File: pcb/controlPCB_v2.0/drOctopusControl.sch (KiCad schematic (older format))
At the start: 74 parts, among them CON1 Servo, CON10 AVR_Prog, CON2 Servo, CON3 Heater, CON4 +12V, CON5 BEC, CON6 PIN-2x2_angled, CON7 FAN1, CON8 FAN2, CON9 UART, Q1 16MHz, SW1 RESET, T1 IRLR2905PBF, T2 IRLML6244TRPBF, T3 IRLML6244TRPBF, T4 IRLML6244TRPBF, U1 ATmega328-AU, U2 78M05CDT, U3 ESP-01, U4 AMS1117-3.3

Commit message: Working on PCBs
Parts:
- removed C11, C12: 470u/16V, Cpol_8.0_12.0_M, symbol Cpol
- removed C13, C15: 100u/25V, Cpol_6.3_11.0_N, symbol Cpol
- removed CON10: AVR_Prog, PIN-2x3_N, symbol AVR_Prog
- removed CON3: Heater, EDG-5.08mm-2_N, symbol EDG-5.08mm-2
- removed CON4: +12V, EDG-5.08mm-2_N, symbol EDG-5.08mm-2
- removed CON5: BEC, EDG-5.08mm-4_N, symbol EDG-5.08mm-4
- removed CON6: PIN-2x2_angled, PIN-2x2_angled_N, symbol PIN-2x2_angled
- removed CON7: FAN1, PIN-1x3_M, symbol PIN-1x3
- removed CON8: FAN2, PIN-1x3_M, symbol PIN-1x3
- removed CON9: UART, PIN-1x6_angled_N, symbol PIN-1x6_angled
- removed D10, D9: PESD5V2S2UT, SOT23-3_N, symbol PESD5V2S2UT
- removed D5, D6, D7, D8: SS14, SMA_N, symbol SS14
- removed Q1: 16MHz, 3.7x3.1_N, symbol Ceramic_3.7x3.1_16MHz
- removed R2: 100R, 0603_N, symbol R
- removed R5: 4k7 1%, 0603_N, symbol R
- removed R8, R9: 22R/1W, 2512_N, symbol R
- removed RN4: 1k, 4x0603_N, symbol R_Network_4
- removed RN5: 22k, 4x0603_N, symbol R_Network_4
- removed SW1: RESET, MicroswitchSmd-4.3_N, symbol MicroswitchSmt-4.3
- removed T1: IRLR2905PBF, D-PAK_N, symbol IRLR2905PBF
- removed U1: ATmega328-AU, QFP-32-0.8_M, symbol ATmega328-AU
- removed U2: 78M05CDT, D-PAK_N, symbol 78M05CDT
- removed U3: ESP-01, ESP-01_N_socket, symbol ESP-01
- added C11, C12, C13, C15, C17, C18, C19: 100n, 0603_N, symbol C
- added CON1: PIN-2x2_F, PIN-2x2_F_N, symbol PIN-2x2_F
- added CON10, CON11: Therm, PIN-2x3_N, symbol PIN-2x3
- added CON4: Outputs, PIN-2x3_N, symbol PIN-2x3
- added CON5: PIN-2x3, PIN-2x3_F_N, symbol PIN-2x3
- added CON6: PIN-2x4, PIN-2x4_F_N, symbol PIN-2x4
- added CON7: PIN-2x4, PIN-2x4_N, symbol PIN-2x4
- added D5, D6: BAS40-05(DIOTEC), SOT23-3_N, symbol BAS40-05
- added MECH9: PowerPCB, niceMechanical:dummy, symbol dummy_mech
- added Q1: Ceramic_3.7x3.1_8Mhz, 3.7x3.1_N, symbol Ceramic_3.7x3.1_8Mhz
- added R2: 10k, 0603_N, symbol R_V
- added RN5, RN6: 10k, 4x0603_N, symbol R_Network_4V
- added RN7, RN8: 10k, 4x0603_N, symbol R_Network_4
- added SW1: Button, MicroswitchSmd6x4_N, symbol MicroswitchSmt6x4_V
- added SW2: Reset, MicroswitchSmd6x4_N, symbol MicroswitchSmt6x4_V
- added U1: STM32F103RBT6, QFP-64-0.5_N, symbol STM32F103RBT6
- added U2: Oled128x64_M, niceModules:Oled128x64_M_5.08N, symbol Oled128x64_M
- CON2: footprint PIN-3x4_angled_N -> nicePinheaders:PIN-3x4_N
- CON3: renamed from CON1; footprint PIN-3x4_angled_N -> nicePinheaders:PIN-3x4_N
- R1: value 100R -> R
- R3: value 100R -> 10k
- R4: value 100R -> 1k
- RN3: value 1k -> 100R
- renumbered CON1 to CON3
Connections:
- net labels added: +3V3, BTN, DBG_RxD, DBG_TxD, ESP_RxD, ESP_TxD, HEATER, RST, SCL, SDA, SWCLK, SWDIO, SWO, Servo0, Servo0a, VDDA, cmd_heater, esp_boot, esp_en, heater_fb, therm0, therm1, therm2, therm3, therm4, therm5, therm6
- net labels removed: #DTR, #ESP, #RxD, #TxD, ESP_BOOT, ESP_EN, ESP_ENa, HEAT, Heater, MISO, MOSI, RESET, SCK, Servo8, Servo8a, Therm, uC_RxD, uC_TxD
- wire segments 220 -> 263
- no-connect marks 5 -> 4
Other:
- note added: "ADC12_IN10"
- note added: "ADC12_IN11"
- note added: "ADC12_IN12"
- note added: "ADC12_IN13"
- note added: "ADC12_IN14"
- note added: "ADC12_IN15"
- note added: "ADC12_IN4"
- note added: "ADC12_IN5"
- note added: "ADC12_IN6"
- note added: "ADC12_IN7"
- note added: "ADC12_IN8"
- note added: "ADC12_IN9"
- note added: "Buzzer\nOLED\ndebug UART\nUSB?"
- note added: "I2C2_SCL"
- note added: "I2C2_SDA"
- note added: "TIM1_CH1"
- note added: "TIM1_CH2"
- note added: "TIM1_CH3"
- note added: "TIM1_CH4"
- note added: "TIM3_CH1"
- note added: "TIM3_CH2"
- note added: "TIM3_CH3"
- note added: "TIM3_CH4"
- note added: "TIM4_CH1"
- note added: "TIM4_CH2"
- note added: "TIM4_CH3"
- note added: "TIM4_CH4"
- note added: "USART2_RX"
- note added: "USART2_TX"
- note added: "USART3_RX"
- note added: "USART3_TX"
- note added: "therm0a"
- note added: "therm1a"
- note added: "therm2a"
- note added: "therm3a"
- note added: "therm4a"
- note added: "therm5a"
- note removed: "#+5V"
- note removed: "4A max.\n0.65W max."
- note removed: "5V±5%\n300mA max.\n1.55W max."
- note removed: "8\n9\n10\n11\n12\n13\nA0\nA1\nA2\nA3\nA4\nA5\n0\n1\n2\n3\n4\n5\n6\n7"
- note removed: "A6\nA7"
- moved on the sheet: CON2A, CON2C, D11, D12, MECH1, MECH2, MECH3, MECH4, MECH5, MECH6, MECH7, MECH8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

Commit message: Schematic polishing
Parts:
- CON1: value PIN-2x2_F -> PowerPCB2
- CON5: value PIN-2x3 -> PowerPCB3
- CON6: value PIN-2x4 -> PowerPCB1
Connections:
- wire segments 263 -> 328
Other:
- note removed: "Buzzer\nOLED\ndebug UART\nUSB?"
- moved on the sheet: C1, C10, C11, C12, C13, C14, C15, C16, C17, C18, C19, C2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

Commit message: Schematic polishing
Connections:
- net LED1: now also U1.33 (PB12)
- net LED2: now also U1.34 (PB13)
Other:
- note added: "3V3 LDO regulator"
- note added: "6V power is for servos\n5V for OLED and LDO\n12V for external outputs"
- note added: "External thermistor inputs"
- note added: "For uC only"
- note added: "Mechanical parts and Power PCB"
- note added: "Medium power outputs"
- note added: "Motor and two fans"
- note added: "Power PCB connectors"
- note added: "Power PCB\nfor 3D model"
- note added: "Programming/debug connector and reset switch"
- note added: "STM32 microcontroller"
- note added: "Servo connectors"
- note added: "Servos powered from external BEC regulator"
- note added: "Thermistor 0 and 3 are for higher temperatures\nand have lower pullup resistances."
- note added: "User interaction"
- moved on the sheet: C1, C10, C11, C12, C13, C14, C15, C16, C17, C18, C19, C2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

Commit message: Schematic polishing
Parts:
- removed C4: 100n, 0603_N, symbol C
- removed R4: 1k, 0603_N, symbol R
- added R4: 1k, 0603_N, symbol R_V
- added R5: 2k2, 0603_N, symbol R
- added R6: 10k, 0603_N, symbol R
- added R7: 10k, 0603_N, symbol R_V
- added RN4: 10k, 4x0603_N, symbol R_Network_4V
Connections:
- net +3V3: no longer RN6.7 (2), RN8.4 (1)
- net BTN: no longer RN8.5 (2)
- net F1: now also D6.2 (A2); no longer D6.1 (A1)
- net F2: now also D6.1 (A1); no longer D6.2 (A2)
- net Fan1: now also RN4.5 (2)
- net Fan2: now also RN4.2 (1), RN4.6 (2), RN4.7 (2)
- net GND: now also R4.1, R7.1, RN4.1, RN4.3 (1), RN4.4 (1)
- net Motor: now also RN4.8 (2)
- net cmd_heater: now also R5.2, R7.2; no longer CON6.6
- net heater_fb: now also R4.2
- net therm0: now also RN7.8 (2); no longer RN7.1
- net therm1: now also RN7.6 (2); no longer RN7.2 (1)
- net therm2: now also RN7.5 (2); no longer RN7.3 (1)
- net therm3: now also RN8.8 (2), U1.11 (PC3); no longer RN8.1, U1.25 (PC5)
- net therm4: now also RN8.6 (2), U1.9 (PC1); no longer RN8.2 (1), U1.26 (PB0)
- net therm5: now also RN8.5 (2), U1.10 (PC2); no longer RN8.3 (1), U1.27 (PB1)
- net at C14.1, CON10.4: now also RN5.3 (1), RN7.3 (1); no longer RN5.2 (1), RN7.7 (2)
- net at C13.1, CON10.6: now also RN5.4 (1), RN7.4 (1); no longer RN5.1, RN7.6 (2)
- net at C17.1, CON11.4: now also RN6.3 (1), RN8.3 (1); no longer RN6.2 (1), RN8.7 (2)
- net at C16.1, CON11.6: now also RN6.4 (1), RN8.4 (1); no longer RN6.1, RN8.6 (2)
- new net: CON6.6, R5.1, R6.1
- new net: C15.1, CON10.2, RN5.1, RN5.2 (1), RN7.1
- new net: C18.1, CON11.2, RN6.1, RN8.1
- new net bts_fb: R6.2, U1.25 (PC5)
- no-connect marks 4 -> 8
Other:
- note added: "ADC12_IN0"
- note added: "ADC12_IN1"
- note added: "THERM0"
- note added: "Thermistor 0 is for higher temperature - for heater\nand have lower pullup resistance.\nOther are for servos and BEC"
- note removed: "Thermistor 0 and 3 are for higher temperatures\nand have lower pullup resistances."
- note removed: "therm0a"
- moved on the sheet: C19, CON4, D5, D6, RN3A, RN3B, RN3C, RN3D, RN5A, RN5B, RN5C, RN5D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

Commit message: PCB routing
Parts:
- added TP1: PA12, pnConnector:TP_1mm, symbol Testpoint
- added TP2: PB14, pnConnector:TP_1mm, symbol Testpoint
- added TP3: PB15, pnConnector:TP_1mm, symbol Testpoint
- added TP4: PA0, pnConnector:TP_1mm, symbol Testpoint
- added TP5: PA1, pnConnector:TP_1mm, symbol Testpoint
- added TP6: PB4, pnConnector:TP_1mm, symbol Testpoint
- added TP7: PB5, pnConnector:TP_1mm, symbol Testpoint
- added TP8: PC0, pnConnector:TP_1mm, symbol Testpoint
- R1, R10, R11, R2, R3, R4, R5, R6, R7: footprint 0603_N -> 0603_R_N
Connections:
- net +3V3: now also RN7.2 (1), RN7.7 (2), RN8.4 (1)
- net +5V: now also CON6.8; no longer CON6.5
- net GND: now also RN4.2 (1); no longer RN4.3 (1)
- net B2B_heater_cmd: now reaches R5.1, R6.1
- net B2B_heater_cmd: now also CON6.5; no longer CON6.6
- net at C17.1, CON11.4, RN6.3 (1): now also RN8.2 (1); no longer RN8.3 (1)
- net at C16.1, CON11.6, RN6.4 (1): now also RN8.3 (1); no longer RN8.4 (1)
- net fan2_cmd: now reaches RN3.2 (1)
- net fan2_cmd: now also RN4.7 (2), U1.39 (PC8)
- net at RN3.7 (2): now also T4.1 (G)
- net at RN3.6 (2): no longer T4.1 (G)
- net B2B_esp_boot: now reaches U1.26 (PB0)
- net B2B_esp_boot: now also CON6.3
- net B2B_esp_en: now reaches U1.27 (PB1)
- net B2B_esp_en: now also CON6.1
- net button_sig: now reaches U1.50 (PA15)
- net button_sig: now also RN8.5 (2), SW1.2
- net therm4_sig: now reaches RN8.7 (2)
- net therm4_sig: now also U1.10 (PC2)
- net BTN: no longer names the net of U1.57 (PB5)
- net BTN: no longer SW1.2
- net ESP_RxD renamed B2B_ESP_RxD
- net B2B_ESP_RxD: now also CON6.4; no longer CON6.3
- net ESP_TxD renamed B2B_ESP_TxD
- net B2B_ESP_TxD: now also CON6.2; no longer CON6.1
- net F1 renamed FAN1_OUT
- net F2 renamed FAN2_OUT
- net Fan1 renamed fan1_cmd
- net fan1_cmd: now also U1.38 (PC7); no longer U1.39 (PC8)
- removed net Fan2: RN3.3 (1), RN4.2 (1), RN4.6 (2), RN4.7 (2), U1.40 (PC9)
- net HEATER renamed B2B_heater_out
- net B2B_heater_out: now also CON6.7; no longer CON6.8
- net LED1 renamed led1_cmd
- net LED2 renamed led2_cmd
- net MOT renamed MOTOR_OUT
- net Motor renamed motor_cmd
- net motor_cmd: now also U1.40 (PC9); no longer U1.38 (PC7)
- net SCL renamed scl
- net SDA renamed sda
- net Servo0 renamed servo0_cmd
- net Servo0a renamed SERVO0_OUT
- net Servo1 renamed servo1_cmd
- net Servo1a renamed SERVO1_OUT
- net Servo2 renamed servo2_cmd
- net Servo2a renamed SERVO2_OUT
- net Servo3 renamed servo3_cmd
- net Servo3a renamed SERVO3_OUT
- net Servo4 renamed servo4_cmd
- net servo4_cmd: now also U1.61 (PB8); no longer U1.58 (PB6)
- net Servo4a renamed SERVO4_OUT
- net Servo5 renamed servo5_cmd
- net Servo5a renamed SERVO5_OUT
- net Servo6 renamed servo6_cmd
- net servo6_cmd: now also U1.58 (PB6); no longer U1.61 (PB8)
- net Servo6a renamed SERVO6_OUT
- net Servo7 renamed servo7_cmd
- net Servo7a renamed SERVO7_OUT
- net bts_fb renamed bts_fb_sig
- net cmd_heater renamed heater_cmd
- net esp_boot: no longer names the net of U1.15 (PA1)
- net esp_boot: no longer CON6.4
- net esp_en: no longer names the net of U1.14 (PA0/WKUP)
- net esp_en: no longer CON6.2
- net heater_fb renamed heater_sig
- net heater_sig: now also U1.21 (PA5); no longer U1.20 (PA4)
- net therm0 renamed therm0_sig
- net therm1 renamed therm1_sig
- net therm2 renamed therm2_sig
- net therm3 renamed therm3_sig
- net therm3_sig: now also U1.9 (PC1); no longer U1.11 (PC3)
- net therm4 renamed therm5_sig
- net therm5_sig: now also U1.11 (PC3); no longer U1.9 (PC1)
- removed net therm5: RN8.5 (2), U1.10 (PC2)
- removed net therm6: CON6.7, U1.21 (PA5)
- new net B2B_therm6_sig: CON6.6, U1.20 (PA4)
- no-connect marks 8 -> 10
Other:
- note added: "Naming convention:\n- small_letters (_cmd,_sig) - board level signals\n (out/in from uC)\n- BIG_LETTERS (_OUT,_IN) - connections to outside world\n- B2B_signals - connections to second board"
- note added: "THERM0_IN"
- note added: "THERM1_IN"
- note added: "THERM2_IN"
- note added: "THERM3_IN"
- note added: "THERM4_IN"
- note added: "THERM5_IN"
- note added: "motor_cmd and two fans"
- note removed: "Motor and two fans"
- note removed: "THERM0"
- note removed: "therm1a"
- note removed: "therm2a"
- note removed: "therm3a"
- note removed: "therm4a"
- note removed: "therm5a"
- moved on the sheet: C10, C14, C15, C17, C18, C7, C8, C9, CON10, CON11, CON2A, CON2B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

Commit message: Probably final version of PCBs
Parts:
- added CON8, CON9: GND, PIN-1x1_L, symbol PIN-1x1
- added MECH10: spacer_M3x5+6, niceMechanical:spacer_2x5_plastic, symbol spacer_M3x5+6
- added SW3: Button, MicroswitchSmd6x4_N, symbol MicroswitchSmt6x4_V
- added TP10: Fan1, pnConnector:TP_1mm, symbol Testpoint
- added TP11: Fan2, pnConnector:TP_1mm, symbol Testpoint
- added TP12: S0, pnConnector:TP_1mm, symbol Testpoint
- added TP13: S1, pnConnector:TP_1mm, symbol Testpoint
- added TP14: S2, pnConnector:TP_1mm, symbol Testpoint
- added TP15: S3, pnConnector:TP_1mm, symbol Testpoint
- added TP16: S4, pnConnector:TP_1mm, symbol Testpoint
- added TP17: S5, pnConnector:TP_1mm, symbol Testpoint
- added TP18: S6, pnConnector:TP_1mm, symbol Testpoint
- added TP19: S7, pnConnector:TP_1mm, symbol Testpoint
- added TP9: Motor, pnConnector:TP_1mm, symbol Testpoint
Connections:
- net +3V3: no longer RN8.4 (1)
- net GND: now also CON8.1, CON9.1, SW3.1
- net fan1_cmd: now also TP10.1
- net fan2_cmd: now also TP11.1
- net motor_cmd: now also TP9.1
- net servo0_cmd: now also TP12.1
- net servo1_cmd: now also TP13.1
- net servo2_cmd: now also TP14.1
- net servo3_cmd: now also TP15.1
- net servo4_cmd: now also TP16.1
- net servo5_cmd: now also TP17.1
- net servo6_cmd: now also TP18.1
- net servo7_cmd: now also TP19.1
- net at U1.14 (PA0/WKUP): now also TP4.1
- net at U1.15 (PA1): now also TP5.1
- net at U1.35 (PB14): now also TP2.1
- net at U1.36 (PB15): now also TP3.1
- net at U1.45 (PA12): now also TP1.1
- net at U1.56 (PB4): now also TP6.1
- net at U1.57 (PB5): now also TP7.1
- net button1_sig: now reaches U1.53 (PC12)
- net button1_sig: now also SW3.2
- net at U1.8 (PC0): now also TP8.1
- net button_sig renamed button0_sig
- net button0_sig: no longer RN8.5 (2)
- no-connect marks 10 -> 13
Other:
- moved on the sheet: C10, C6, C9, CON2A, CON2B, CON2C, CON3A, CON3B, CON3C, CON7, D1, D11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

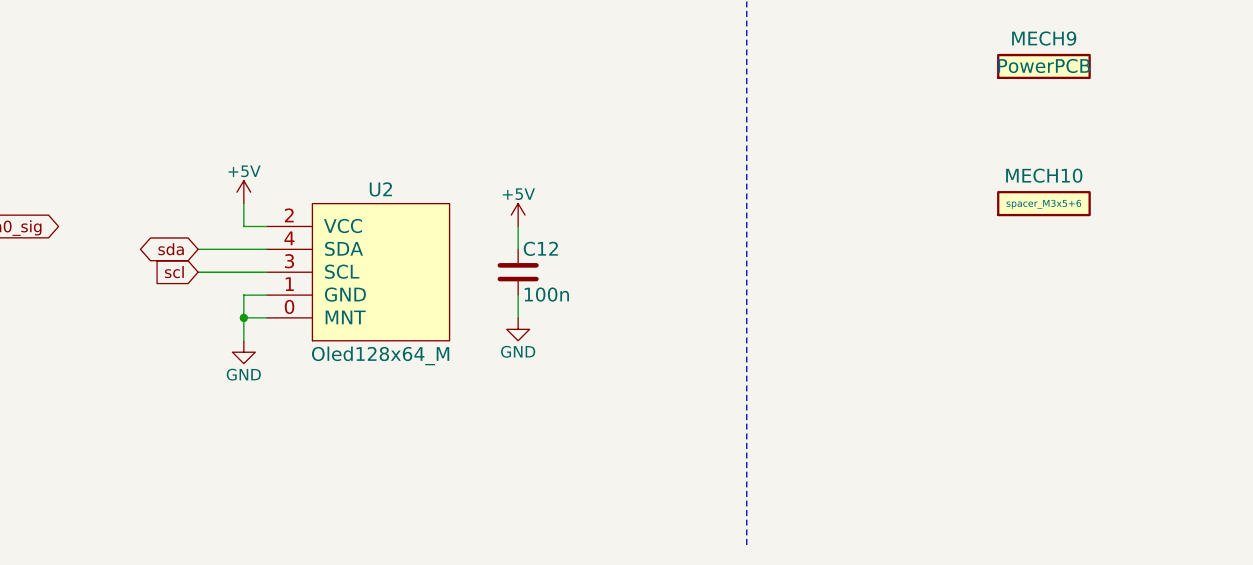
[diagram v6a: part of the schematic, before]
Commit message: Mechanical parts added
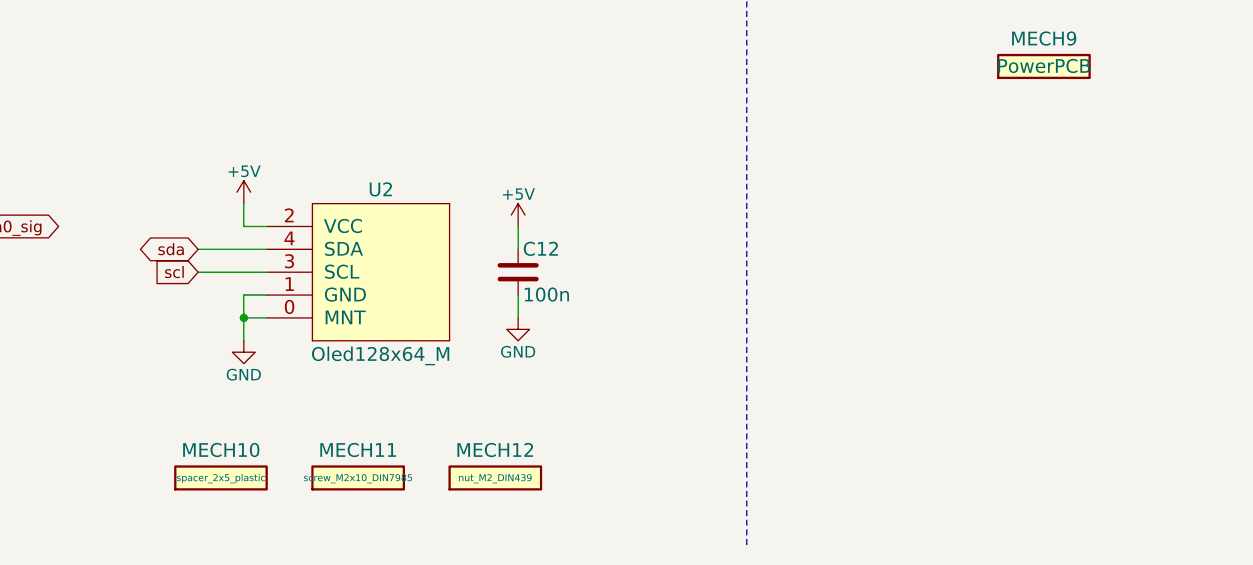
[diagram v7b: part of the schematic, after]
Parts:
- added MECH11: screw_M2x10_DIN7985, niceMechanical:screw_M2x10_DIN7985, symbol spacer_M3x5+6
- added MECH12: nut_M2_DIN439, niceMechanical:nut_M2_DIN439, symbol spacer_M3x5+6
- MECH10: value spacer_M3x5+6 -> spacer_2x5_plastic
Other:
- moved on the sheet: MECH10
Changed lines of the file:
@@
 L spacer_M3x5+6 MECH10
 U 1 1 56B4B14A
-P 12300 9700
-F 0 "MECH10" H 12300 9820 60  0000 C CNN
-F 1 "spacer_M3x5+6" H 12300 9700 30  0000 C CNN
-F 2 "niceMechanical:spacer_2x5_plastic" H 12300 9610 40  0001 C CNN
-F 3 "" H 12300 9700 60  0000 C CNN
-	1    12300 9700
+P 8700 10900
+F 0 "MECH10" H 8700 11020 60  0000 C CNN
+F 1 "spacer_2x5_plastic" H 8700 10900 30  0000 C CNN
+F 2 "niceMechanical:spacer_2x5_plastic" H 8700 10810 40  0001 C CNN
+F 3 "" H 8700 10900 60  0000 C CNN
+	1    8700 10900
 	1    0    0    -1
 $EndComp
+$Comp
+L spacer_M3x5+6 MECH11
+U 1 1 56B4D301
+P 9300 10900
+F 0 "MECH11" H 9300 11020 60  0000 C CNN
+F 1 "screw_M2x10_DIN7985" H 9300 10900 30  0000 C CNN
+F 2 "niceMechanical:screw_M2x10_DIN7985" H 9300 10810 40  0001 C CNN
+F 3 "" H 9300 10900 60  0000 C CNN
+	1    9300 10900
+	1    0    0    -1
+$EndComp
+$Comp
+L spacer_M3x5+6 MECH12
+U 1 1 56B4D5C7
+P 9900 10900
+F 0 "MECH12" H 9900 11020 60  0000 C CNN
+F 1 "nut_M2_DIN439" H 9900 10900 30  0000 C CNN
+F 2 "niceMechanical:nut_M2_DIN439" H 9900 10810 40  0001 C CNN
+F 3 "" H 9900 10900 60  0000 C CNN
+	1    9900 10900
+	1    0    0    -1
+$EndComp
